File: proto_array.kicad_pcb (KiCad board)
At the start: 2 copper layers, 99.1 x 129.5 mm, 55 parts, among them P1 CONN_01X03, U1 ADS131E08, U2 BEAGLEBONEBLACK

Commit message: Update PCB.
* Remove test point
* Add header to PRU pins

Signed-off-by: Chamon <luizchamon@gmail.com>
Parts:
- removed TP1: TESTPOINT, Measurement_Points:Measurement_Point_Round-SMD-Pad_Big
- added P2: CONN_01X02, micarray:Pin_Header_01x02, B.Cu at (89.2, 119.4)
- added P3: CONN_01X02, micarray:Pin_Header_01x02, B.Cu at (89.2, 134.6)
- added P4: CONN_01X02, micarray:Pin_Header_01x02, B.Cu at (89.2, 123.2)
- added P5: CONN_01X02, micarray:Pin_Header_01x02, B.Cu at (89.2, 127.0)
- added P6: CONN_01X02, micarray:Pin_Header_01x02, B.Cu at (89.2, 111.8)
- added P7: CONN_01X02, micarray:Pin_Header_01x02, B.Cu at (89.2, 130.8)
- added P8: CONN_01X02, micarray:Pin_Header_01x02, B.Cu at (89.2, 115.6)
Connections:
- U1 pad 34: /PRU1_0 -> Net-(P6-Pad1)
- U1 pad 36: /PRU1_2 -> Net-(P8-Pad1)
- U1 pad 38: /PRU1_4 -> Net-(P2-Pad1)
- U1 pad 39: /PRU1_7 -> Net-(P4-Pad1)
- U1 pad 40: /PRU1_5 -> Net-(P5-Pad1)
- U1 pad 43: /PRU1_3 -> Net-(P7-Pad1)
- U1 pad 47: /PRU1_1 -> Net-(P3-Pad1)
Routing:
- net AGND: track 21.7 -> 100.3 mm, vias 0 -> 4
- net Net-(P3-Pad1): track 0.00 -> 71.3 mm
- net Net-(P7-Pad1): track 0.00 -> 65.1 mm
- net Net-(P5-Pad1): track 0.00 -> 59.1 mm
- net Net-(P4-Pad1): track 0.00 -> 53.5 mm
- net Net-(P2-Pad1): track 0.00 -> 47.9 mm
- net Net-(P8-Pad1): track 0.00 -> 42.5 mm
- net Net-(P6-Pad1): track 0.00 -> 35.5 mm
- net /PRU1_1: track 62.1 -> 33.0 mm
- net /PRU1_3: track 56.2 -> 28.2 mm
- net /PRU1_5: track 50.5 -> 23.3 mm
- net /PRU1_7: track 44.7 -> 18.5 mm
- net /PRU1_4: track 44.3 -> 23.4 mm
- net /PRU1_0: track 42.8 -> 22.6 mm
- net /PRU1_2: track 42.5 -> 23.7 mm
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- added copper zone on B.Cu, net AGND
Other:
- board text removed: "An airwire is required between the digital ground pours."

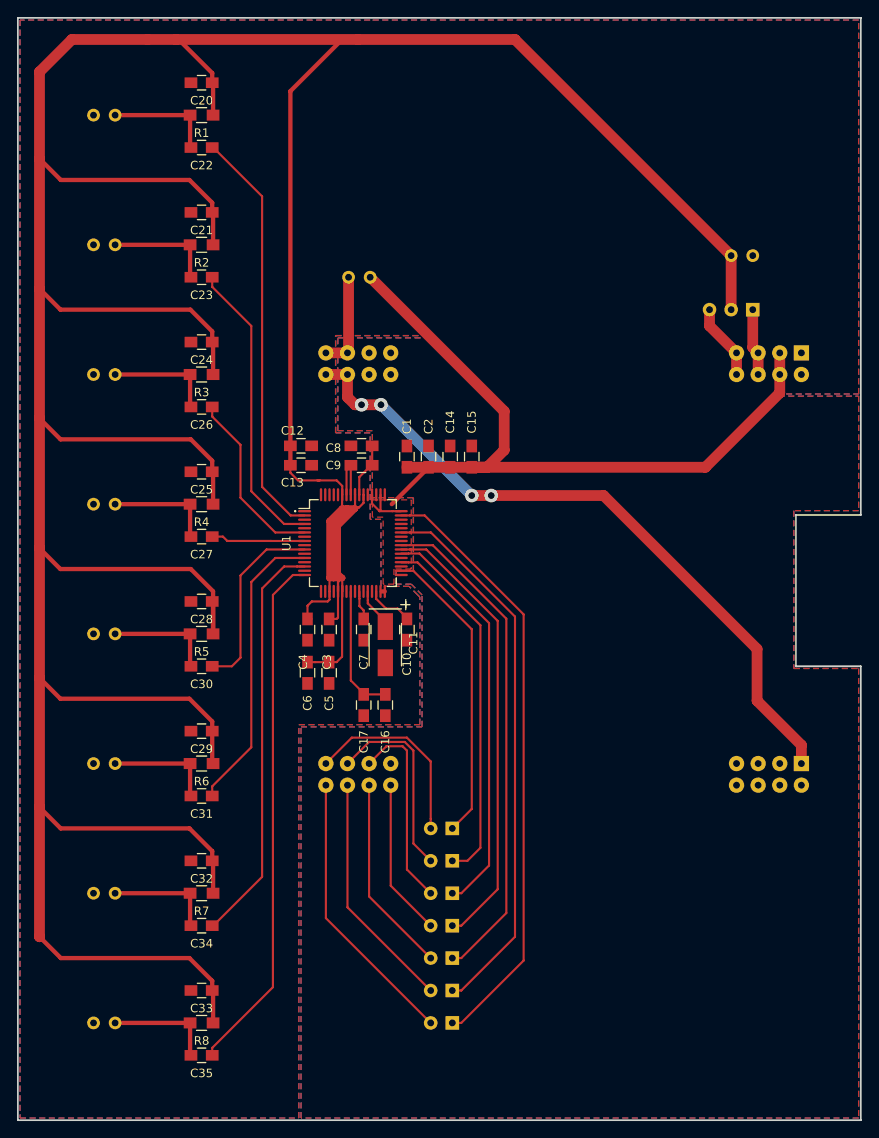
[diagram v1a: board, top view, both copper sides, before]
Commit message: Update PCB with new changes in schematics.
Signed-off-by: Chamon <luizchamon@gmail.com>
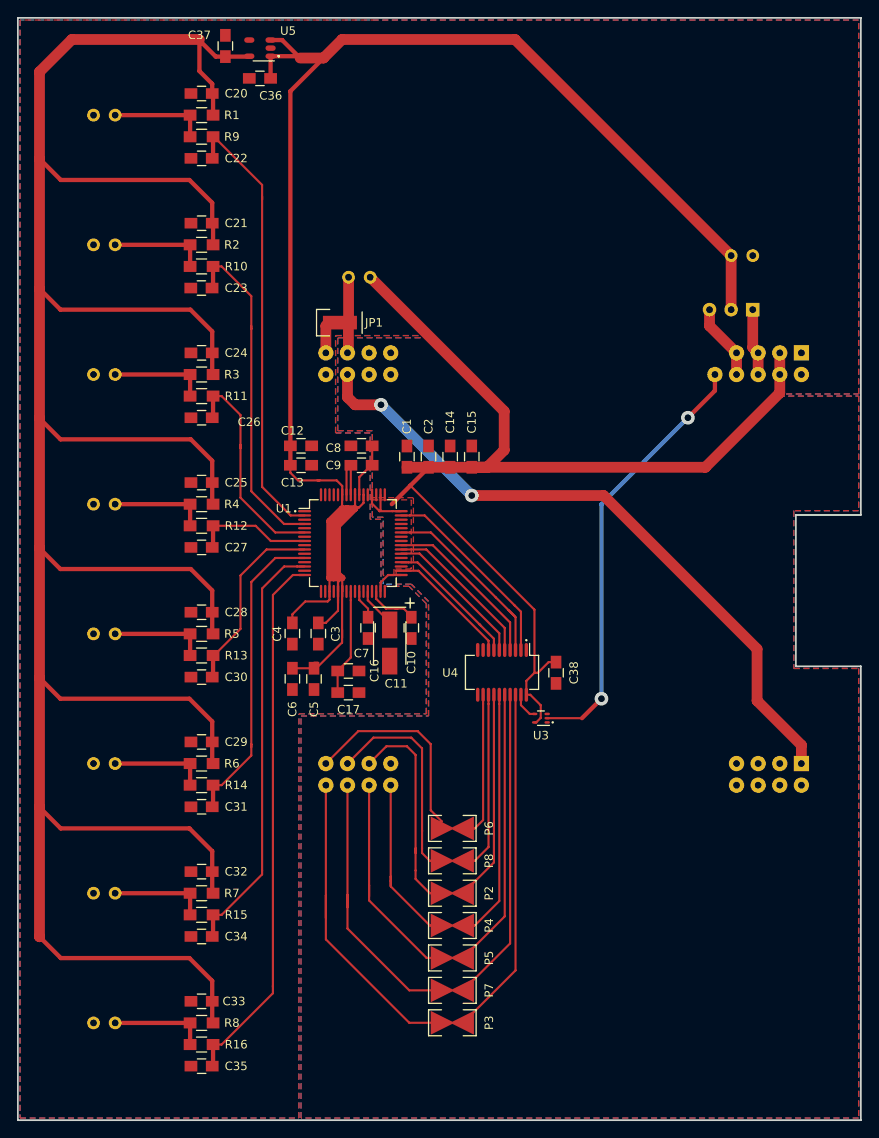
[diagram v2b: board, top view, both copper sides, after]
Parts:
- added C36: 1uF, Capacitors_SMD:C_0805_HandSoldering, F.Cu at (66.5, 23.6)
- added C37: 1uF, Capacitors_SMD:C_0805_HandSoldering, F.Cu at (62.5, 19.8)
- added C38: 1uF, Capacitors_SMD:C_0805_HandSoldering, F.Cu at (101.3, 93.5)
- added JP1: JUMPER, micarray:Jumper, F.Cu at (75.9, 52.3)
- added R10: 10k, Resistors_SMD:R_0805_HandSoldering, F.Cu at (59.7, 45.7)
- added R11: 10k, Resistors_SMD:R_0805_HandSoldering, F.Cu at (59.7, 61.0)
- added R12: 10k, Resistors_SMD:R_0805_HandSoldering, F.Cu at (59.7, 76.2)
- added R13: 10k, Resistors_SMD:R_0805_HandSoldering, F.Cu at (59.7, 91.4)
- added R14: 10k, Resistors_SMD:R_0805_HandSoldering, F.Cu at (59.7, 106.7)
- added R15: 10k, Resistors_SMD:R_0805_HandSoldering, F.Cu at (59.7, 121.9)
- added R16: 10k, Resistors_SMD:R_0805_HandSoldering, F.Cu at (59.7, 137.2)
- added R9: 10k, Resistors_SMD:R_0805_HandSoldering, F.Cu at (59.7, 30.5)
- added U3: 741G04, micarray:SOTFL-5_160x50_Pitch0.5, F.Cu at (99.6, 98.8)
- added U4: 743245, micarray:SOP-20_600x175_Pitch0.635, F.Cu at (95.0, 93.4)
- added U5: TLV70233DBV, micarray:SOT-23-5, F.Cu at (66.5, 20.1)
- P2, P3, P4, P5, P6, P7, P8: footprint micarray:Pin_Header_01x02 -> micarray:Pin_Header_NC_01x02; moved to F.Cu
- moved C16 5.90 mm to (76.9, 93.3), turned to 0 degrees
- moved C17 2.32 mm to (76.9, 95.8), turned to 0 degrees
- moved C5 1.91 mm to (72.9, 94.2)
- moved C6 1.91 mm to (70.4, 94.2)
- moved C4 1.84 mm to (70.4, 88.9)
- moved C3 1.35 mm to (73.4, 88.9)
- moved C23 1.27 mm to (59.7, 48.3), turned to 0 degrees
- moved C25 1.27 mm to (59.7, 71.1)
- moved C30 1.27 mm to (59.7, 94.0), turned to 0 degrees
- moved C32 1.27 mm to (59.7, 116.8)
- moved C33 1.27 mm to (59.7, 132.1)
- moved C21 1.27 mm to (59.7, 40.6)
- moved C22 1.27 mm to (59.7, 33.0), turned to 0 degrees
- moved C24 1.27 mm to (59.7, 55.9)
- moved C26 1.27 mm to (59.7, 63.5), turned to 0 degrees
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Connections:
- C1 pad 2: AGND -> DGND
- C14 pad 2: AGND -> DGND
- C15 pad 2: AGND -> DGND
- C19 pad 2: AGND -> DGND
- C2 pad 2: AGND -> DGND
- C20 pad 1: AVDD -> +3V3
- C21 pad 1: AVDD -> +3V3
- C22 pad 1: /MIC_1 -> AGND
- C22 pad 2: Net-(C22-Pad2) -> /MIC_1
- C23 pad 1: /MIC_2 -> AGND
- C23 pad 2: Net-(C23-Pad2) -> /MIC_2
- C24 pad 1: AVDD -> +3V3
- C25 pad 1: AVDD -> +3V3
- C26 pad 1: /MIC_3 -> AGND
- C26 pad 2: Net-(C26-Pad2) -> /MIC_3
- C27 pad 1: /MIC_4 -> AGND
- C27 pad 2: Net-(C27-Pad2) -> /MIC_4
- C28 pad 1: AVDD -> +3V3
- C29 pad 1: AVDD -> +3V3
- C30 pad 1: /MIC_5 -> AGND
- C30 pad 2: Net-(C30-Pad2) -> /MIC_5
- C31 pad 1: /MIC_6 -> AGND
- C31 pad 2: Net-(C31-Pad2) -> /MIC_6
- C32 pad 1: AVDD -> +3V3
- C33 pad 1: AVDD -> +3V3
- C34 pad 1: /MIC_7 -> AGND
- C34 pad 2: Net-(C34-Pad2) -> /MIC_7
- C35 pad 1: /MIC_8 -> AGND
- C35 pad 2: Net-(C35-Pad2) -> /MIC_8
- MIC1 pad 1: Net-(C22-Pad2) -> Net-(MIC1-Pad1)
- MIC2 pad 1: Net-(C23-Pad2) -> Net-(MIC2-Pad1)
- MIC3 pad 1: Net-(C26-Pad2) -> Net-(MIC3-Pad1)
- MIC4 pad 1: Net-(C27-Pad2) -> Net-(MIC4-Pad1)
- MIC5 pad 1: Net-(C30-Pad2) -> Net-(MIC5-Pad1)
- MIC6 pad 1: Net-(C31-Pad2) -> Net-(MIC6-Pad1)
- MIC7 pad 1: Net-(C34-Pad2) -> Net-(MIC7-Pad1)
- MIC8 pad 1: Net-(C35-Pad2) -> Net-(MIC8-Pad1)
- R1 pad 1: AVDD -> +3V3
- R1 pad 2: Net-(C22-Pad2) -> Net-(MIC1-Pad1)
- R2 pad 1: AVDD -> +3V3
- R2 pad 2: Net-(C23-Pad2) -> Net-(MIC2-Pad1)
- R3 pad 1: AVDD -> +3V3
- R3 pad 2: Net-(C26-Pad2) -> Net-(MIC3-Pad1)
- R4 pad 1: AVDD -> +3V3
- R4 pad 2: Net-(C27-Pad2) -> Net-(MIC4-Pad1)
- R5 pad 1: AVDD -> +3V3
- R5 pad 2: Net-(C30-Pad2) -> Net-(MIC5-Pad1)
- R6 pad 1: AVDD -> +3V3
- R6 pad 2: Net-(C31-Pad2) -> Net-(MIC6-Pad1)
- R7 pad 1: AVDD -> +3V3
- R7 pad 2: Net-(C34-Pad2) -> Net-(MIC7-Pad1)
- R8 pad 1: AVDD -> +3V3
- R8 pad 2: Net-(C35-Pad2) -> Net-(MIC8-Pad1)
- U1 pad 31: AGND -> DGND
- U1 pad 33: AGND -> DGND
- U1 pad 34: Net-(P6-Pad1) -> /ADS_DIN
- U1 pad 36: Net-(P8-Pad1) -> /ADS_RESET
- U1 pad 38: Net-(P2-Pad1) -> /ADS_START
- U1 pad 39: Net-(P4-Pad1) -> /ADS_CS
- U1 pad 40: Net-(P5-Pad1) -> /ADS_SCLK
- U1 pad 43: Net-(P7-Pad1) -> /ADS_DOUT
- U1 pad 47: Net-(P3-Pad1) -> /ADS_DRDY
- U1 pad 49: AGND -> DGND
- U1 pad 51: AGND -> DGND
- U2 pad B1: AGND -> DGND
- U2 pad B2: AGND -> DGND
- U2 pad C10: Net-(U2-PadC10) -> /SYS_RESETn
- U2 pad C43: AGND -> DGND
- U2 pad C44: AGND -> DGND
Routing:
- net +3V3: track 0.00 -> 330.8 mm
- net AVDD: track 537.8 -> 209.2 mm
- net DGND: track 0.00 -> 91.6 mm, vias 0 -> 2
- net AGND: track 100.3 -> 11.1 mm, vias 4 -> 0
- net /SYS_RESETn: track 0.00 -> 51.0 mm, vias 0 -> 2
- net DVDD: track 98.8 -> 137.5 mm
- net Net-(P3-Pad1): track 71.3 -> 41.1 mm
- net Net-(P7-Pad1): track 65.1 -> 37.0 mm
- net Net-(P5-Pad1): track 59.1 -> 33.0 mm
- net Net-(P4-Pad1): track 53.5 -> 29.7 mm
- net /ADS_DRDY: track 0.00 -> 23.3 mm
- net Net-(P2-Pad1): track 47.9 -> 24.8 mm
- net /ADS_DOUT: track 0.00 -> 22.5 mm
- net Net-(P8-Pad1): track 42.5 -> 21.6 mm
- net /ADS_SCLK: track 0.00 -> 19.8 mm
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- added copper zone on B.Cu, net DGND
- added copper zone on F.Cu, net DGND
